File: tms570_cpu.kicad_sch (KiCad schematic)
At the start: 51 parts, among them J2 CONN_02X05, U2 TMS570LS0914PGE

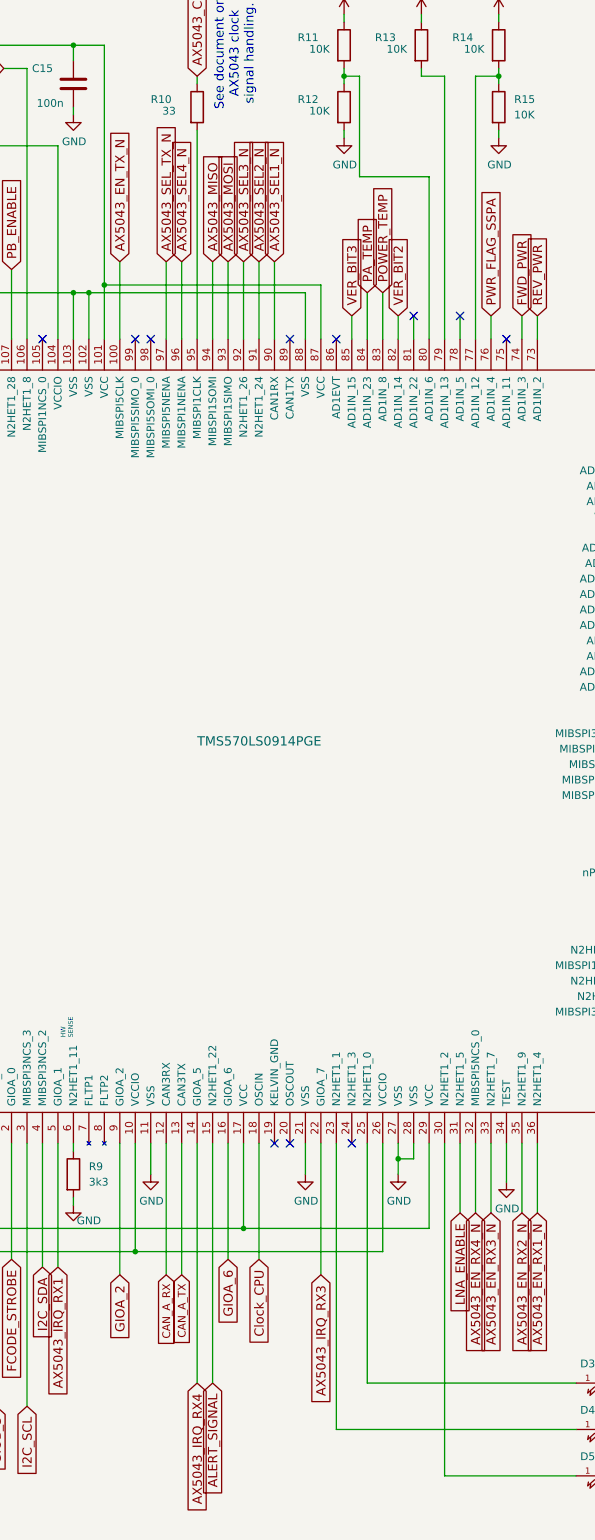
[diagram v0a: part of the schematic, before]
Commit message: Move some pins around and start on the README
Move pins so that MIBSPI5 is available for use in the future.

Signed-off-by: Corey Minyard <corey@minyard.net>
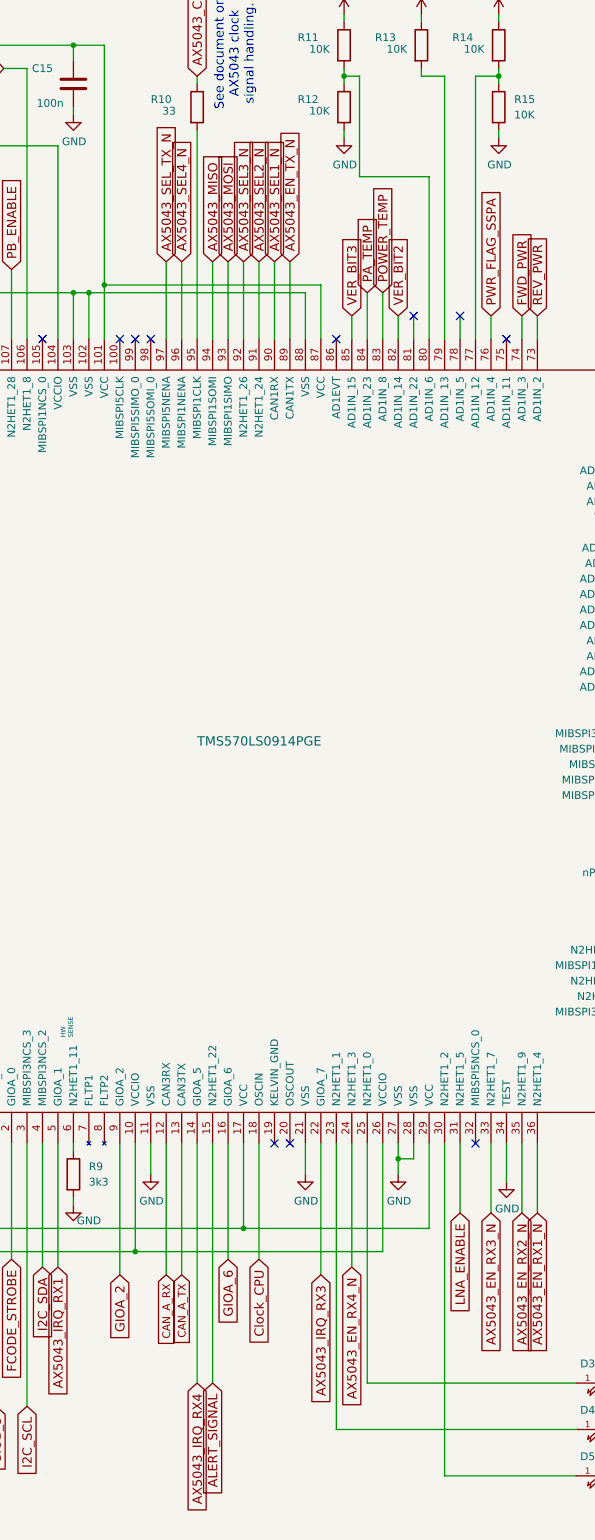
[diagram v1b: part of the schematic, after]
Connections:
- net AX5043_EN_RX4_N: now also U2.24 (N2HET1_3); no longer U2.32 (MIBSPI5NCS_0)
- net AX5043_EN_TX_N: now also U2.89 (CAN1TX); no longer U2.100 (MIBSPI5CLK)
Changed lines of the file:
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@@
 	)
 	(no_connect
+		(at 250.19 204.47)
+	)
+	(no_connect
 		(at 281.94 182.88)
 	)
@@
 	)
 	(no_connect
-		(at 194.31 72.39)
+		(at 191.77 72.39)
 	)
 	(no_connect
-		(at 229.87 204.47)
+		(at 194.31 72.39)
 	)
 	(no_connect
@@
 	)
 	(no_connect
-		(at 219.71 72.39)
-	)
-	(no_connect
 		(at 281.94 93.98)
 	)
@@
 	(wire
 		(pts
+			(xy 229.87 204.47) (xy 229.87 224.79)
+		)
+		(stroke
+			(width 0)
+			(type default)
+		)
+	)
+	(wire
+		(pts
 			(xy 176.53 27.94) (xy 172.72 27.94)
 		)
@@
 	(wire
 		(pts
-			(xy 191.77 59.69) (xy 191.77 72.39)
-		)
-		(stroke
-			(width 0)
-			(type default)
-		)
-	)
-	(wire
-		(pts
 			(xy 105.41 67.31) (xy 97.79 67.31)
 		)
@@
 	(wire
 		(pts
-			(xy 250.19 204.47) (xy 250.19 215.9)
-		)
-		(stroke
-			(width 0)
-			(type default)
-		)
-	)
-	(wire
-		(pts
 			(xy 152.4 218.44) (xy 212.09 218.44)
 		)
@@
 	(wire
 		(pts
+			(xy 219.71 59.69) (xy 219.71 72.39)
+		)
+		(stroke
+			(width 0)
+			(type default)
+		)
+	)
+	(wire
+		(pts
 			(xy 364.49 162.56) (xy 364.49 165.1)
 		)
@@
 		)
 	)
-	(global_label "FAULT_N"
+	(global_label "AX5043_EN_RX4_N"
 		(shape input)
-		(at 93.98 116.84 180)
+		(at 229.87 224.79 270)
 		(fields_autoplaced yes)
 		(effects
@@
 		)
 		(property "Intersheetrefs" "${INTERSHEET_REFS}"
-			(at 81.9169 116.84 0)
+			(at 229.87 248.6323 90)
 			(effects
 				(font
@@
 		)
 	)
-	(global_label "USB_Suspend_Low"
+	(global_label "FAULT_N"
 		(shape input)
-		(at 133.35 175.26 180)
+		(at 93.98 116.84 180)
 		(fields_autoplaced yes)
 		(effects
@@
 		)
 		(property "Intersheetrefs" "${INTERSHEET_REFS}"
-			(at 110.0382 175.26 0)
+			(at 81.9169 116.84 0)
 			(effects
 				(font
@@
 		)
 	)
-	(global_label "UART_TX1"
+	(global_label "USB_Suspend_Low"
 		(shape input)
-		(at 312.42 177.8 0)
+		(at 133.35 175.26 180)
 		(fields_autoplaced yes)
 		(effects
@@
 				(size 1.524 1.524)
 			)
-			(justify left)
+			(justify right)
 		)
 		(property "Intersheetrefs" "${INTERSHEET_REFS}"
-			(at 325.9344 177.8 0)
+			(at 110.0382 175.26 0)
 			(effects
 				(font
 					(size 1.27 1.27)
 				)
-				(justify left)
+				(justify right)
 				(hide yes)
 			)
 		)
 	)
-	(global_label "AX5043_EN_RX3_N"
+	(global_label "UART_TX1"
 		(shape input)
-		(at 252.73 215.9 270)
+		(at 312.42 177.8 0)
 		(fields_autoplaced yes)
 		(effects
@@
 				(size 1.524 1.524)
 			)
-			(justify right)
+			(justify left)
 		)
 		(property "Intersheetrefs" "${INTERSHEET_REFS}"
-			(at 252.73 239.7423 90)
+			(at 325.9344 177.8 0)
 			(effects
 				(font
 					(size 1.27 1.27)
 				)
-				(justify right)
+				(justify left)
 				(hide yes)
 			)
 		)
 	)
-	(global_label "AX5043_EN_TX_N"
+	(global_label "AX5043_EN_RX3_N"
 		(shape input)
-		(at 191.77 59.69 90)
+		(at 252.73 215.9 270)
 		(fields_autoplaced yes)
 		(effects
@@
 				(size 1.524 1.524)
 			)
-			(justify left)
+			(justify right)
 		)
 		(property "Intersheetrefs" "${INTERSHEET_REFS}"
-			(at 191.77 37.662 90)
+			(at 252.73 239.7423 90)
 			(effects
 				(font
 					(size 1.27 1.27)
 				)
-				(justify left)
+				(justify right)
 				(hide yes)
 			)
@@
 		)
 	)
+	(global_label "AX5043_EN_TX_N"
+		(shape input)
+		(at 219.71 59.69 90)
+		(fields_autoplaced yes)
+		(effects
+			(font
+				(size 1.524 1.524)
+			)
+			(justify left)
+		)
+		(property "Intersheetrefs" "${INTERSHEET_REFS}"
+			(at 219.71 37.662 90)
+			(effects
+				(font
+					(size 1.27 1.27)
+				)
+				(justify left)
+				(hide yes)
+			)
+		)
+	)
 	(global_label "AX5043_SEL3_N"
 		(shape input)
@@
 			(effects
 				(font
-					(size 1.27 1.27)
-				)
-				(justify right)
-				(hide yes)
-			)
-		)
-	)
-	(global_label "AX5043_EN_RX4_N"
-		(shape input)
-		(at 250.19 215.9 270)
-		(fields_autoplaced yes)
-		(effects
-			(font
-				(size 1.524 1.524)
-			)
-			(justify right)
-		)
-		(property "Intersheetrefs" "${INTERSHEET_REFS}"
-			(at 250.19 239.7423 90)
-			(effects
-				(font

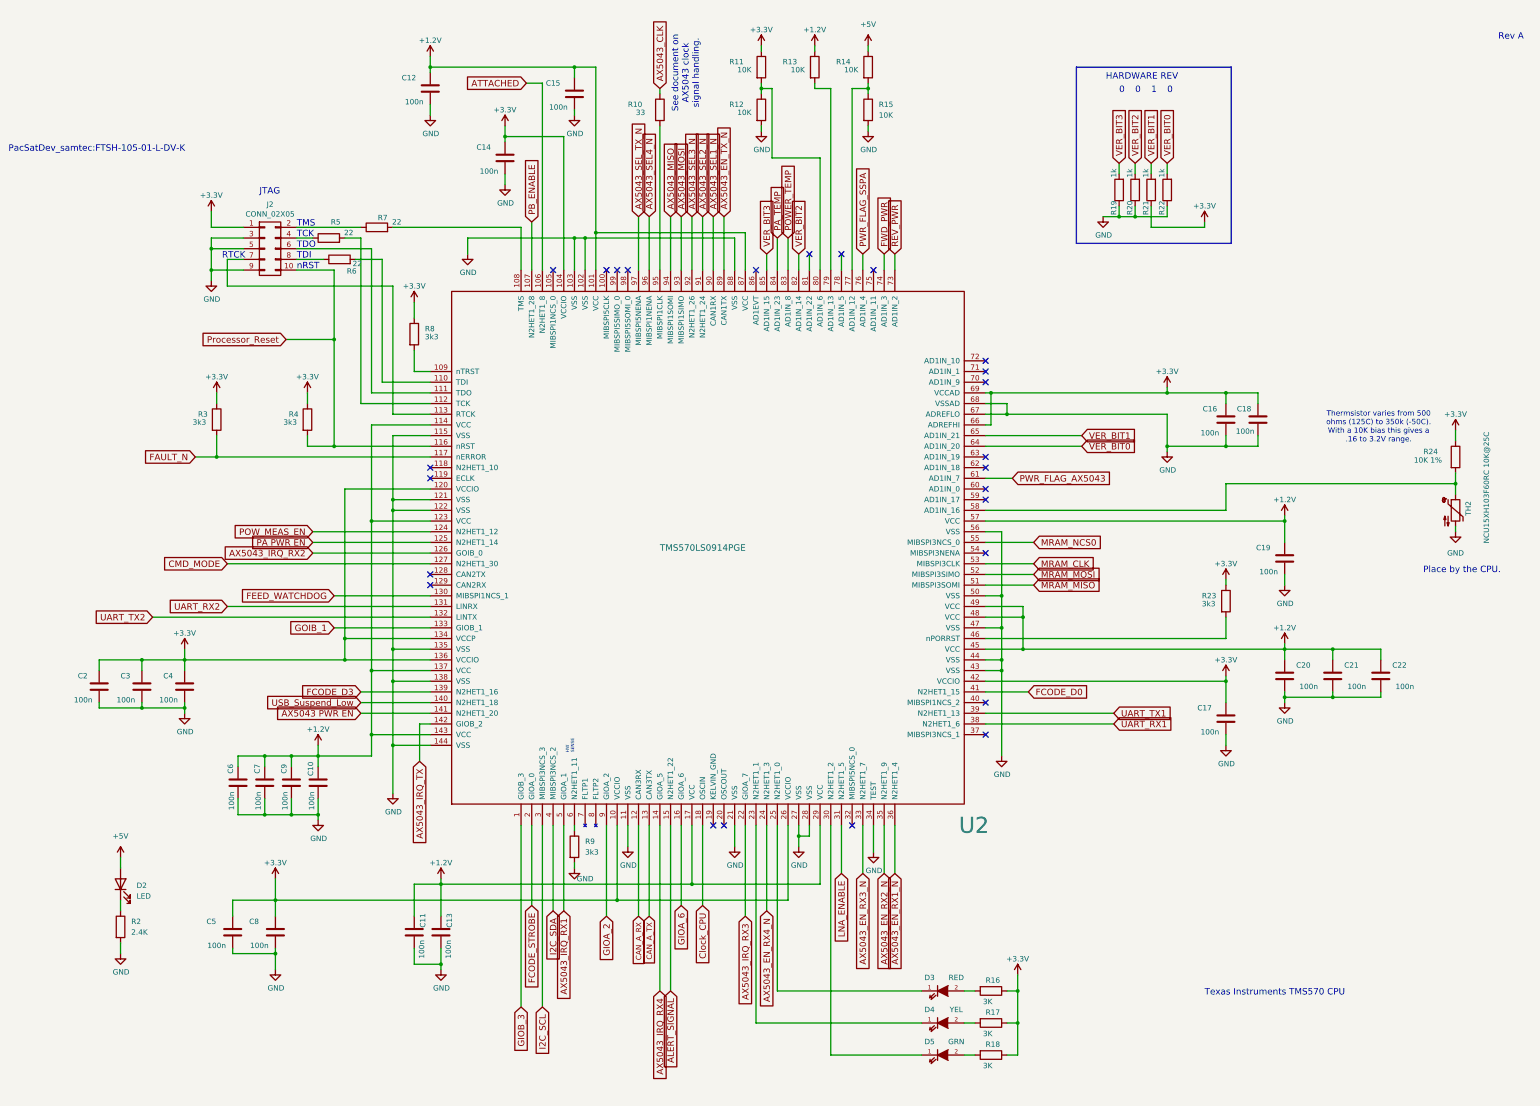
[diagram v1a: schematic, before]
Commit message: Minor adjustments to values and impedance match simulation
Signed-off-by: Corey Minyard <corey@minyard.net>
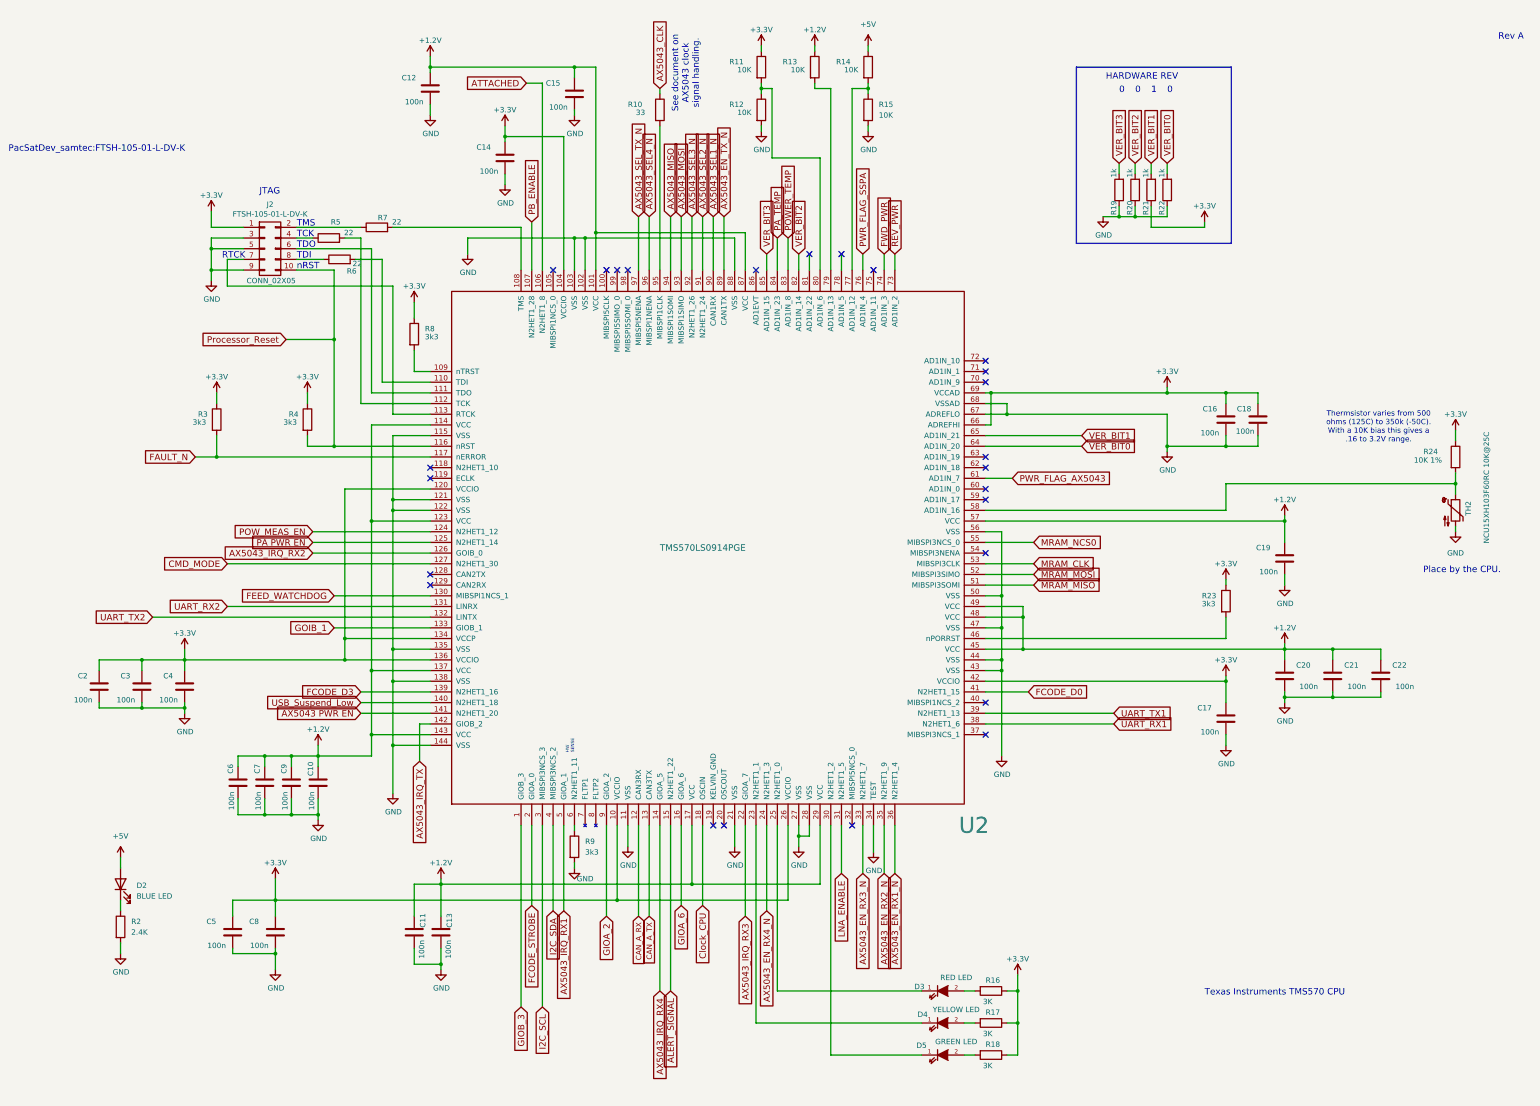
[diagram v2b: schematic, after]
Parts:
- D2: value LED -> BLUE LED
- D3: value RED -> RED LED
- D4: value YEL -> YELLOW LED
- D5: value GRN -> GREEN LED
- J2: value CONN_02X05 -> FTSH-105-01-L-DV-K
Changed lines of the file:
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@@
 			)
 		)
-		(property "Value" "CONN_02X05"
+		(property "Value" "FTSH-105-01-L-DV-K"
 			(at 111.76 59.0804 0)
 			(effects
@@
 			)
 		)
-		(property "Description" ""
-			(at 111.76 67.31 0)
+		(property "Description" "CONN_02X05"
+			(at 112.014 74.93 0)
 			(effects
 				(font
@@
 		(dnp no)
 		(property "Reference" "D3"
-			(at 268.605 240.665 0)
-			(effects
-				(font
-					(size 1.27 1.27)
-				)
-			)
-		)
-		(property "Value" "RED"
+			(at 266.192 242.824 0)
+			(effects
+				(font
+					(size 1.27 1.27)
+				)
+			)
+		)
+		(property "Value" "RED LED"
 			(at 274.955 240.665 0)
 			(effects
@@
 		(dnp no)
 		(property "Reference" "D4"
-			(at 268.605 248.285 0)
-			(effects
-				(font
-					(size 1.27 1.27)
-				)
-			)
-		)
-		(property "Value" "YEL"
+			(at 266.954 249.428 0)
+			(effects
+				(font
+					(size 1.27 1.27)
+				)
+			)
+		)
+		(property "Value" "YELLOW LED"
 			(at 274.955 248.285 0)
 			(effects
@@
 		(dnp no)
 		(property "Reference" "D5"
-			(at 268.605 255.905 0)
-			(effects
-				(font
-					(size 1.27 1.27)
-				)
-			)
-		)
-		(property "Value" "GRN"
+			(at 266.7 256.794 0)
+			(effects
+				(font
+					(size 1.27 1.27)
+				)
+			)
+		)
+		(property "Value" "GREEN LED"
 			(at 274.955 255.905 0)
 			(effects
@@
 			)
 		)
-		(property "Value" "LED"
+		(property "Value" "BLUE LED"
 			(at 80.01 221.2975 90)
 			(effects

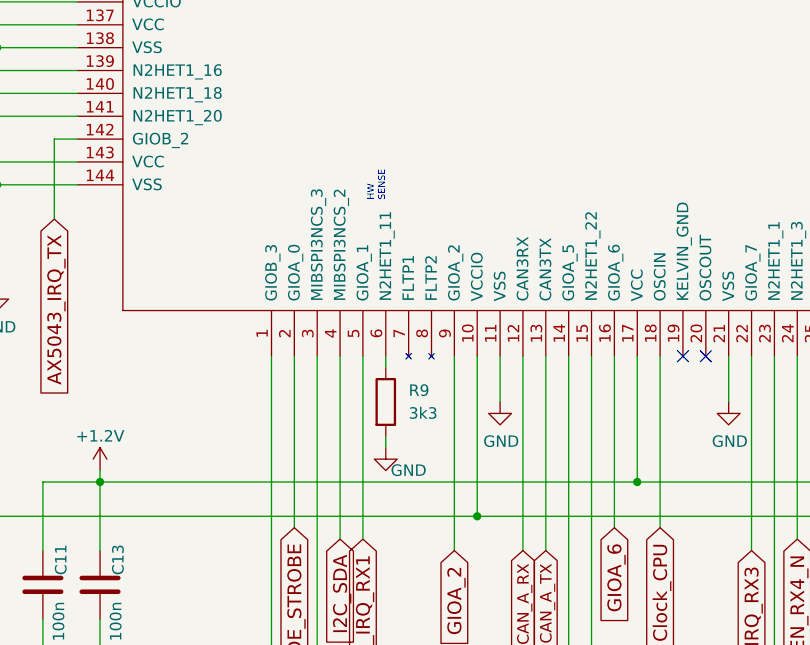
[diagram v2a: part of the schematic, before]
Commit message: Remove the HW_SENSE line
It's not necessary in our setup.

Signed-off-by: Corey Minyard <corey@minyard.net>
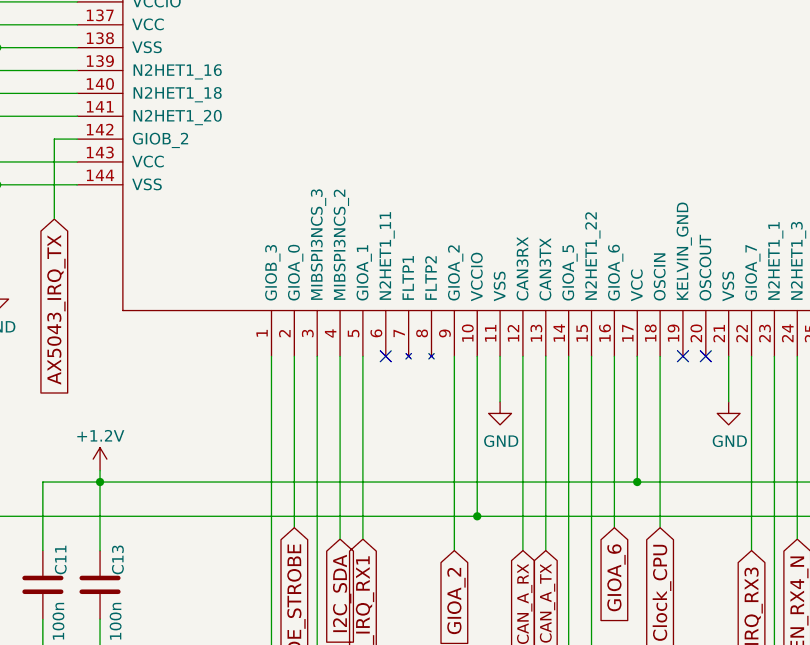
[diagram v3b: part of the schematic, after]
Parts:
- removed R9: 3k3, Resistor_SMD:R_0603_1608Metric_Pad0.98x0.95mm_HandSolder, symbol Device:R
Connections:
- no-connect marks 25 -> 26
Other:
- note removed: "HW SENSE"
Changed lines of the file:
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@@
 		)
 	)
-	(text "HW\nSENSE"
-		(exclude_from_sim no)
-		(at 184.15 187.325 90)
-		(effects
-			(font
-				(size 0.762 0.762)
-			)
-			(justify left bottom)
-		)
-	)
 	(text "0"
 		(exclude_from_sim no)
@@
 	)
 	(no_connect
+		(at 184.15 204.47)
+	)
+	(no_connect
 		(at 149.86 144.78)
 	)
@@
 	(wire
 		(pts
-			(xy 184.15 213.36) (xy 184.15 214.63)
-		)
-		(stroke
-			(width 0)
-			(type default)
-		)
-	)
-	(wire
-		(pts
 			(xy 140.97 162.56) (xy 140.97 170.18)
 		)
@@
 	(wire
 		(pts
-			(xy 184.15 204.47) (xy 184.15 205.74)
-		)
-		(stroke
-			(width 0)
-			(type default)
-		)
-	)
-	(wire
-		(pts
 			(xy 237.49 204.47) (xy 237.49 207.01)
 		)
@@
 	(symbol
 		(lib_id "power:GND")
-		(at 184.15 214.63 0)
-		(unit 1)
-		(exclude_from_sim no)
-		(in_bom yes)
-		(on_board yes)
-		(dnp no)
-		(property "Reference" "#PWR025"
-			(at 184.15 220.98 0)
-			(effects
-				(font
-					(size 1.27 1.27)
-				)
-				(hide yes)
-			)
-		)
-		(property "Value" "GND"
-			(at 186.69 217.17 0)
-			(effects
-				(font
-					(size 1.27 1.27)
-				)
-			)
-		)
-		(property "Footprint" ""
-			(at 184.15 214.63 0)
-			(effects
-				(font
-					(size 1.27 1.27)
-				)
-				(hide yes)
-			)
-		)
-		(property "Datasheet" ""
-			(at 184.15 214.63 0)
-			(effects
-				(font
-					(size 1.27 1.27)
-				)
-				(hide yes)
-			)
-		)
-		(property "Description" ""
-			(at 184.15 214.63 0)
-			(effects
-				(font
-					(size 1.27 1.27)
-				)
-			)
-		)
-		(pin "1"
-		)
-		(instances
-			(project "PacSat_Dev_RevD_240614"
-				(path "/cc9f42d2-6985-41ac-acab-5ab7b01c5b38/adf61ae3-df77-4e04-8bda-b4049a36fcf4"
-					(reference "#PWR025")
-					(unit 1)
-				)
-			)
-		)
-	)
-	(symbol
-		(lib_id "power:GND")
 		(at 309.88 59.69 0)
 		(unit 1)
@@
 					(unit 1)
 				)
-			)
-		)
-	)
-	(symbol
-		(lib_id "Device:R")
-		(at 184.15 209.55 0)
-		(unit 1)
-		(exclude_from_sim no)
-		(in_bom yes)
-		(on_board yes)
-		(dnp no)
-		(property "Reference" "R9"
-			(at 186.69 208.28 0)
-			(effects
-				(font
-					(size 1.27 1.27)
-				)
-				(justify left)
-			)
-		)
-		(property "Value" "3k3"
-			(at 186.69 210.82 0)
-			(effects
-				(font
-					(size 1.27 1.27)
-				)
-				(justify left)
-			)
-		)
-		(property "Footprint" "Resistor_SMD:R_0603_1608Metric_Pad0.98x0.95mm_HandSolder"
-			(at 182.372 209.55 90)
-			(effects
-				(font
-					(size 1.27 1.27)
-				)
-				(hide yes)
-			)
-		)
-		(property "Datasheet" "~"
-			(at 184.15 209.55 0)
-			(effects
-				(font
-					(size 1.27 1.27)
-				)
-			)
-		)
-		(property "Description" ""
-			(at 184.15 209.55 0)
-			(effects
-				(font
-					(size 1.27 1.27)
-				)
-			)
-		)
-		(pin "1"
-		)
-		(pin "2"
-		)
-		(instances
-			(project "PacSat_Dev_RevD_240614"
-				(path "/cc9f42d2-6985-41ac-acab-5ab7b01c5b38/adf61ae3-df77-4e04-8bda-b4049a36fcf4"
-					(reference "R9")
-					(unit 1)
-				)
